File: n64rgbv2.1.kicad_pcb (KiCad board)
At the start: 2 copper layers, 61.2 x 32.8 mm, 89 parts, among them J11 SolderJumper_3_Open, J12 SolderJumper_3_Open, J2 SolderJumper_2_Open, J21 SolderJumper_2_Open, J3 30310-6002HB, J31 SolderJumper_2_Open, U1 EPM570T100, U2 ADV7125, U3 TSH122ICT, U4 TLV70018_SOT23-5, U5 TLV70033_SOT23-5

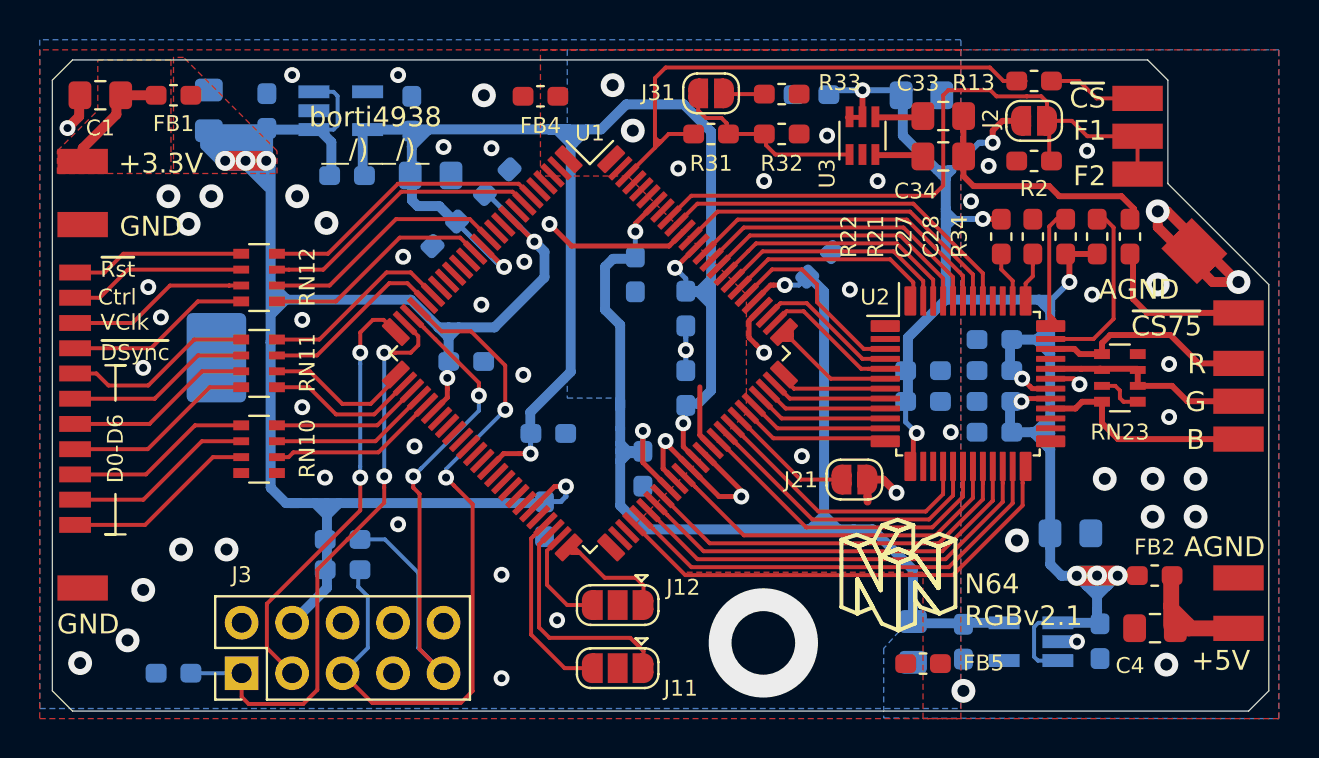
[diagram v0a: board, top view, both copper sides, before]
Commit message: misc updates: - update KiCad to v6 - add SMD footprint for JTAG connector
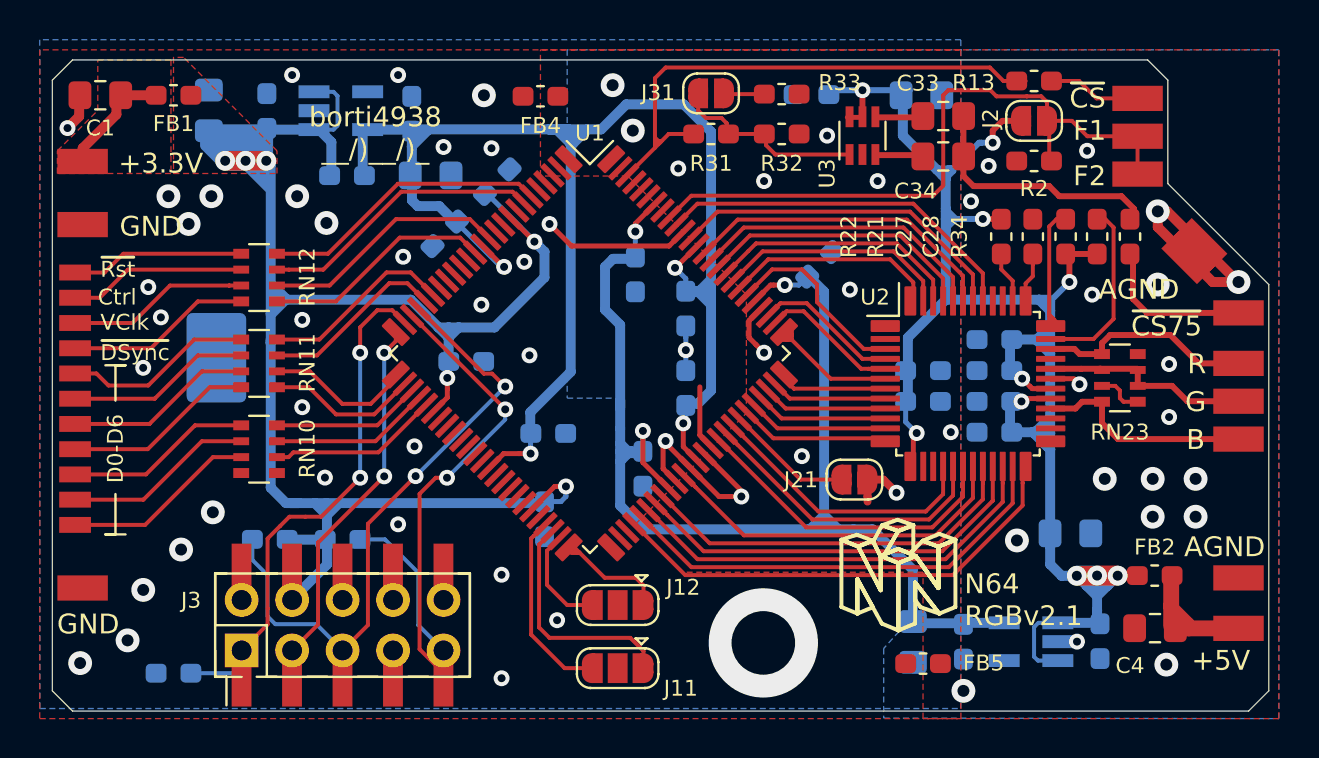
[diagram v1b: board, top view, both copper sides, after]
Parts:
- added J3b1: 30310-6002HB, Connector_PinHeader_2.54mm:PinHeader_2x05_P2.54mm_Vertical_SMD, F.Cu at (128.3, 116.6)
- moved R11 3.97 mm to (124.6, 112.3), turned to 180 degrees
- moved J3 1.14 mm to (123.2, 117.9)
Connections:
- net /~15b_mode_t renamed /~{15b_mode_t}
- net /~BLANK renamed /~{BLANK}
- net /~CSYNC renamed /~{CSYNC}
- net /~CSYNC_75_pre renamed /~{CSYNC_75_pre}
- net /~SYNC renamed /~{SYNC}
- net /~SoG renamed /~{SoG}
- net ~CLAMP renamed ~{CLAMP}
- net ~CSYNC_75_o renamed ~{CSYNC_75_o}
- net ~CSYNC_LVTTL_o renamed ~{CSYNC_LVTTL_o}
- net ~HSYNC renamed ~{HSYNC}
- net ~VSYNC renamed ~{VSYNC}
- J3 pad 6: Net-(J3-Pad6) -> unconnected-(J3-Pad6)
- J3 pad 7: Net-(J3-Pad7) -> unconnected-(J3-Pad7)
- J3 pad 8: Net-(J3-Pad8) -> unconnected-(J3-Pad8)
- RN10 pad 4: Net-(RN10-Pad4) -> unconnected-(RN10-Pad4)
- RN10 pad 5: Net-(RN10-Pad5) -> unconnected-(RN10-Pad5)
- U1 pad 15: Net-(U1-Pad15) -> unconnected-(U1-Pad15)
- U1 pad 16: Net-(U1-Pad16) -> unconnected-(U1-Pad16)
- U1 pad 17: Net-(U1-Pad17) -> unconnected-(U1-Pad17)
- U1 pad 18: Net-(U1-Pad18) -> unconnected-(U1-Pad18)
- U1 pad 19: Net-(U1-Pad19) -> unconnected-(U1-Pad19)
- U1 pad 2: Net-(U1-Pad2) -> unconnected-(U1-Pad2)
- U1 pad 3: Net-(U1-Pad3) -> unconnected-(U1-Pad3)
- U1 pad 33: Net-(U1-Pad33) -> unconnected-(U1-Pad33)
- U1 pad 34: Net-(U1-Pad34) -> unconnected-(U1-Pad34)
- U1 pad 35: Net-(U1-Pad35) -> unconnected-(U1-Pad35)
- U1 pad 36: Net-(U1-Pad36) -> unconnected-(U1-Pad36)
- U1 pad 38: Net-(U1-Pad38) -> unconnected-(U1-Pad38)
- U1 pad 4: Net-(U1-Pad4) -> unconnected-(U1-Pad4)
- U1 pad 40: Net-(U1-Pad40) -> unconnected-(U1-Pad40)
- U1 pad 41: Net-(U1-Pad41) -> unconnected-(U1-Pad41)
- U1 pad 42: Net-(U1-Pad42) -> unconnected-(U1-Pad42)
- U1 pad 43: Net-(U1-Pad43) -> unconnected-(U1-Pad43)
- U1 pad 44: Net-(U1-Pad44) -> unconnected-(U1-Pad44)
- U1 pad 5: Net-(U1-Pad5) -> unconnected-(U1-Pad5)
- U1 pad 51: Net-(U1-Pad51) -> unconnected-(U1-Pad51)
- U1 pad 52: Net-(U1-Pad52) -> unconnected-(U1-Pad52)
- U1 pad 53: Net-(U1-Pad53) -> unconnected-(U1-Pad53)
- U1 pad 96: Net-(U1-Pad96) -> unconnected-(U1-Pad96)
- U4 pad 4: Net-(U4-Pad4) -> unconnected-(U4-Pad4)
- U5 pad 4: Net-(U5-Pad4) -> unconnected-(U5-Pad4)
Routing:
- net TMS: track 37.0 -> 31.3 mm
- net TDO: track 21.9 -> 18.2 mm
- net TCK: track 29.7 -> 26.9 mm
- net +3.3VADC: track 96.0 -> 96.6 mm
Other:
- net class Default removed
- net class Signals removed
- board text added: "N64RGBv2.1.20220409"
- board text added: "~{CS75}"
- board text added: "~{CS}"
- board text added: "~{DSync}"
- board text added: "~{Rst}"
- board text removed: "N64RGBv2.1.20200809"
- board text removed: "~CS"
- board text removed: "~CS75"
- board text removed: "~DSync"
- board text removed: "~Rst"
